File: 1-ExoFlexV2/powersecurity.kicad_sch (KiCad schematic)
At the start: 21 parts, among them J1 24V, J3 24V, K1 UD2-5NU, U1 PTSM36ADBZR, U3 STPS20M100SG-TR, U4 SN74LVC3G14DCUT_V2, U5 CD4044BPWR

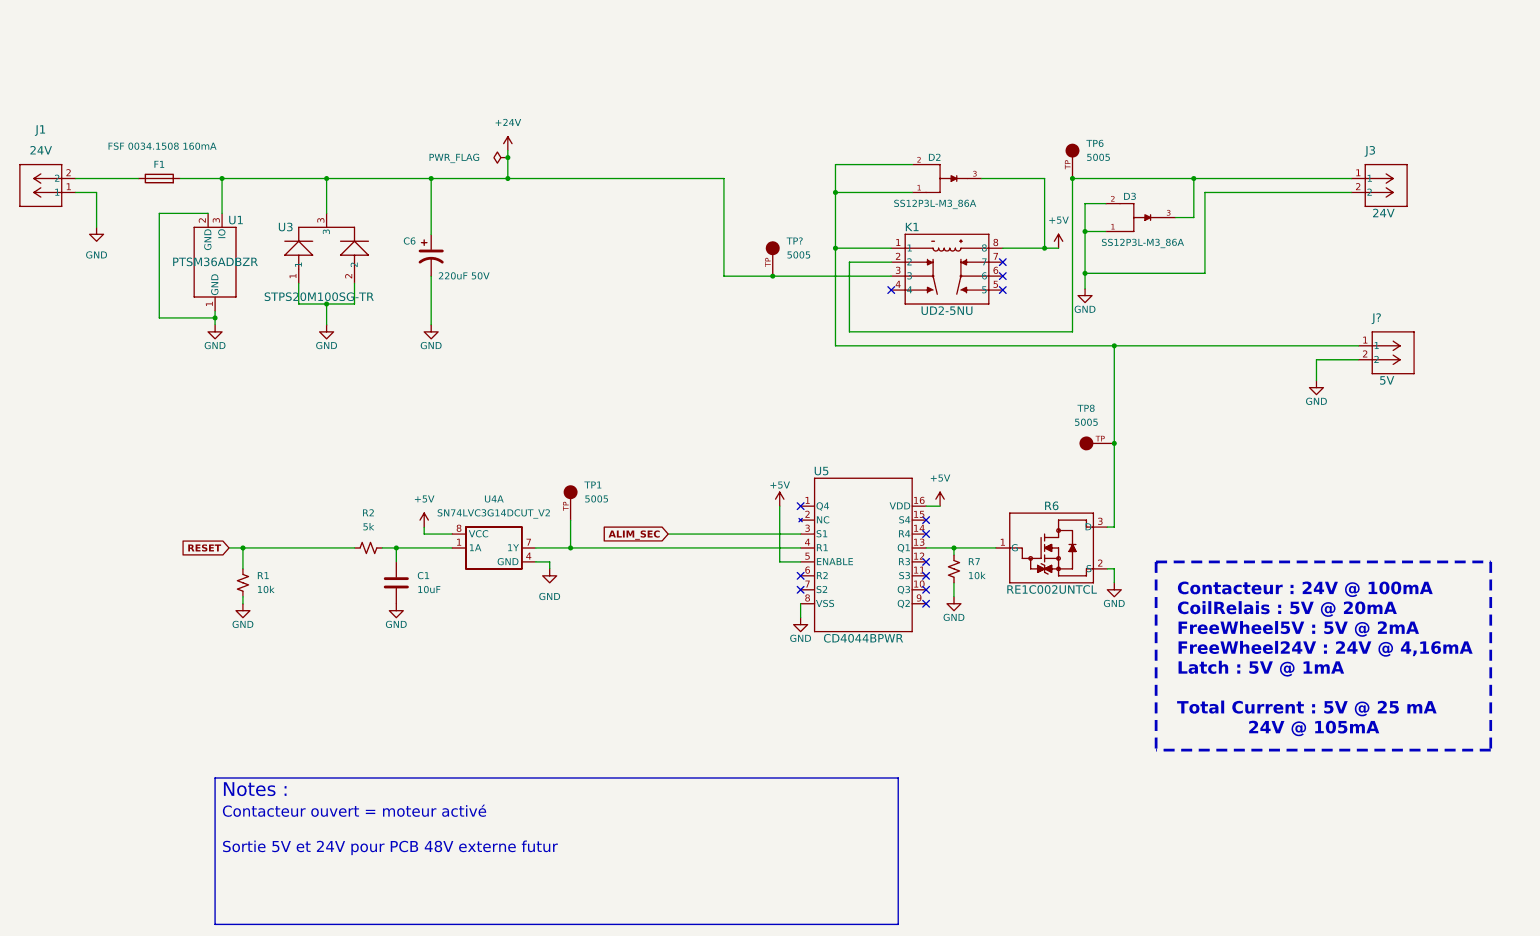
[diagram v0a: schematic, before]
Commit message: Chokes et RC
- Ajout des RF chokes
- Changement des résistance pour 0805
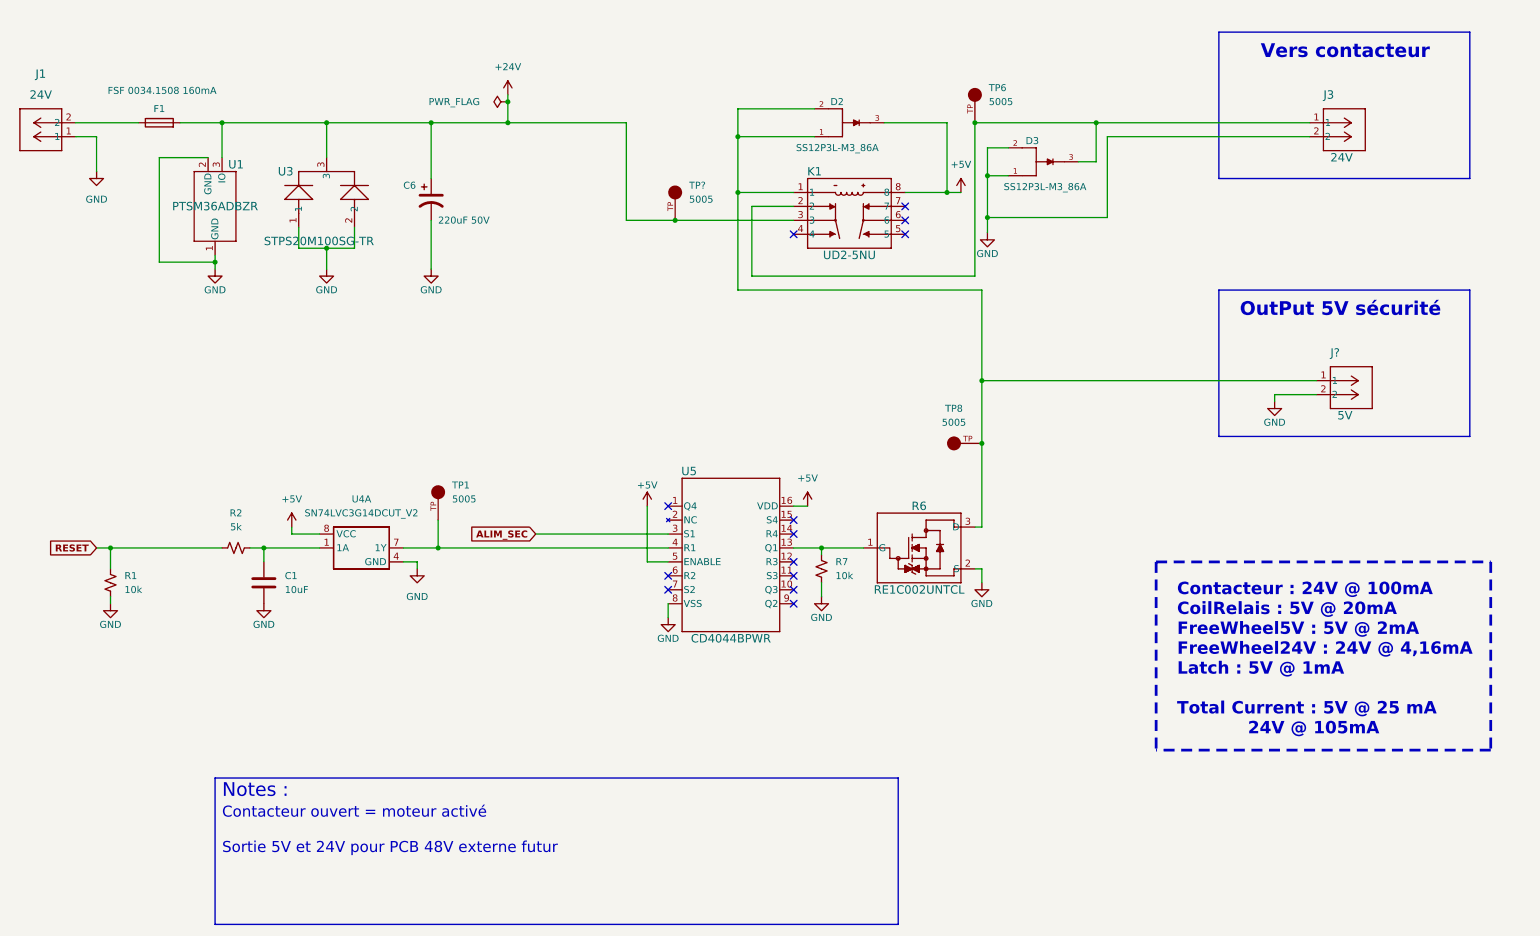
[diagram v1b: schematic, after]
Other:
- note added: "OutPut 5V sécurité"
- note added: "Vers contacteur"
- moved on the sheet: C1, C6, D2, D3, F1, J1, J3, J?, K1, R1, R2, R6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

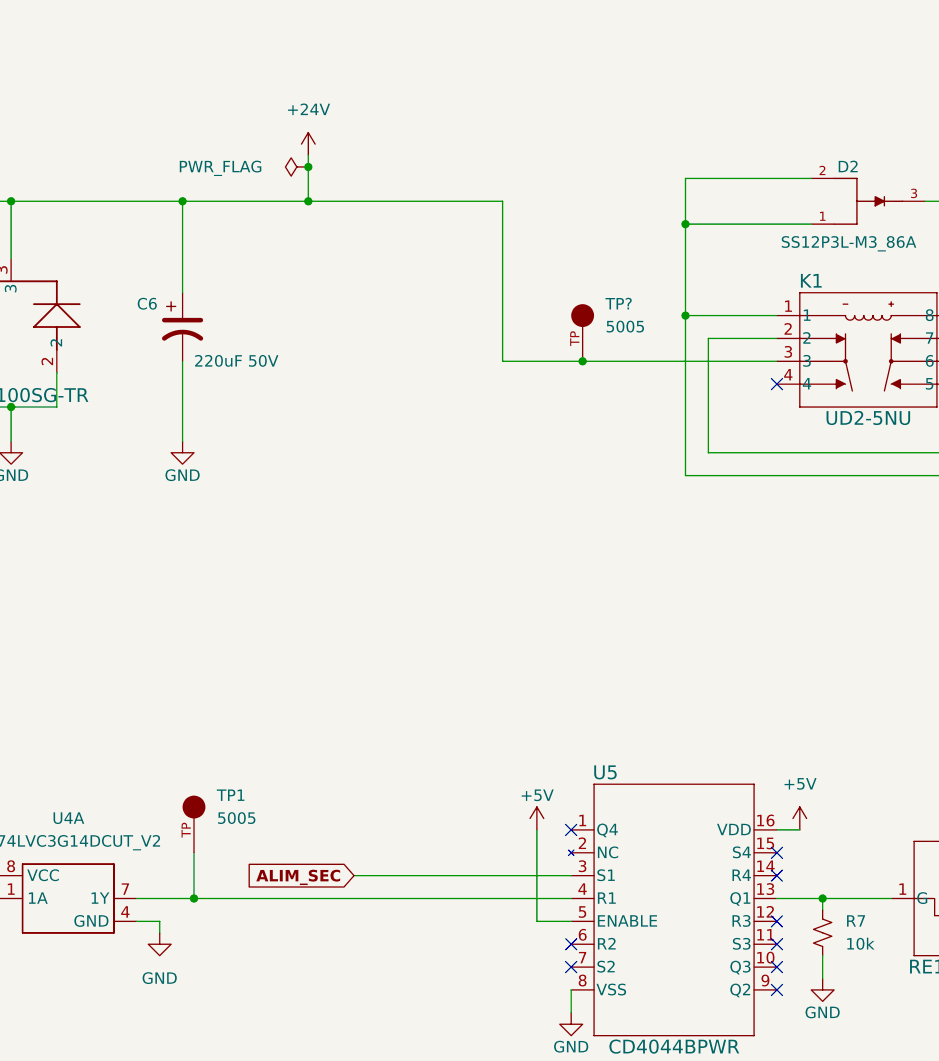
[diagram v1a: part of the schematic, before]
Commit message: Trimmer et jumper
-Changement de symbole de jumper
-Ajout des des trimmer aux endroits nécessaires
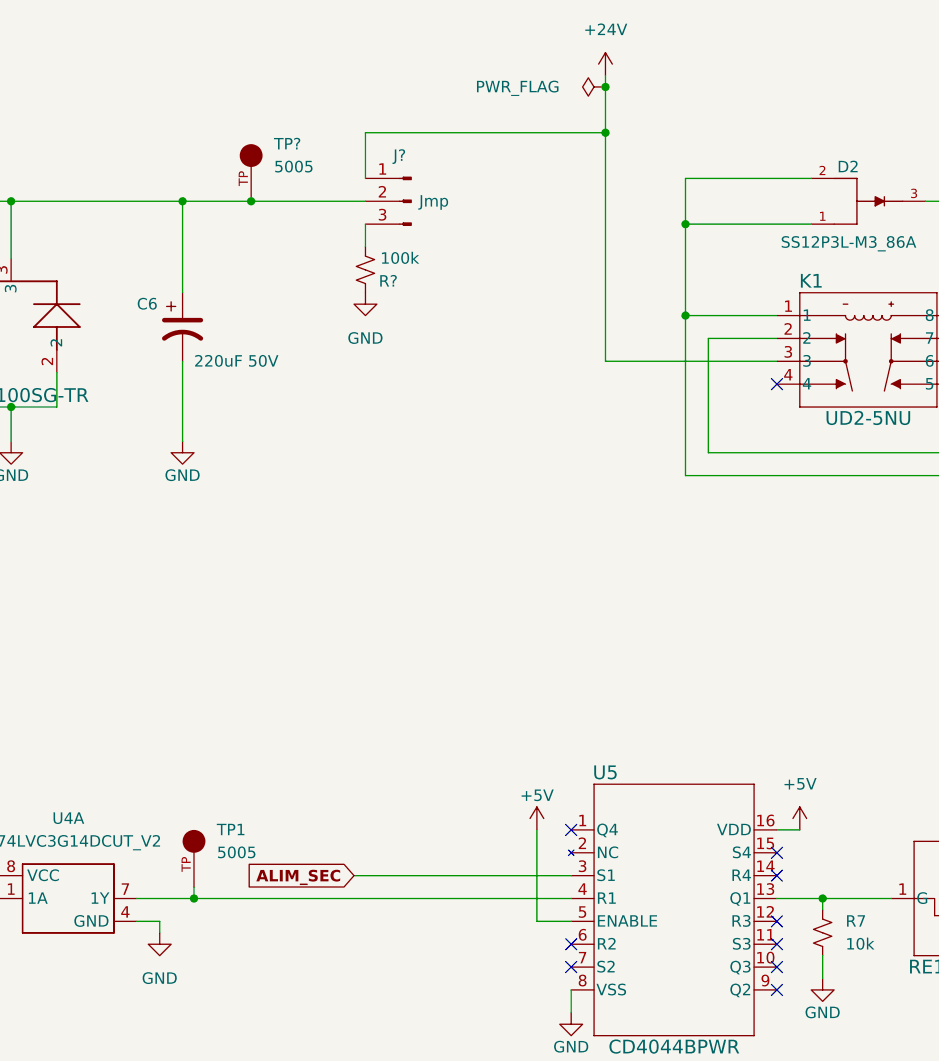
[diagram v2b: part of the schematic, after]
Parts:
- removed TP?: 5005, FootPrint:KEYSTONE_5005, symbol SymLib:5005
- added J?: Jmp, symbol Connector:Conn_01x03_Male
- added R?: 100k, Resistor_SMD:R_0805_2012Metric, symbol Device:R_Small_US
- added TP?: 5005, FootPrint:KEYSTONE_5005, symbol SymLib:5005
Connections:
- net +24V: now also J?.1 (Pin_1); no longer C6.1, F1.2, U1.3 (IO), U3.3
- net GND: now also R?.2
- new net: C6.1, F1.2, J?.2 (Pin_2), TP?.TP, U1.3 (IO), U3.3
- new net: J?.3 (Pin_3), R?.1
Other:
- moved on the sheet: TP1

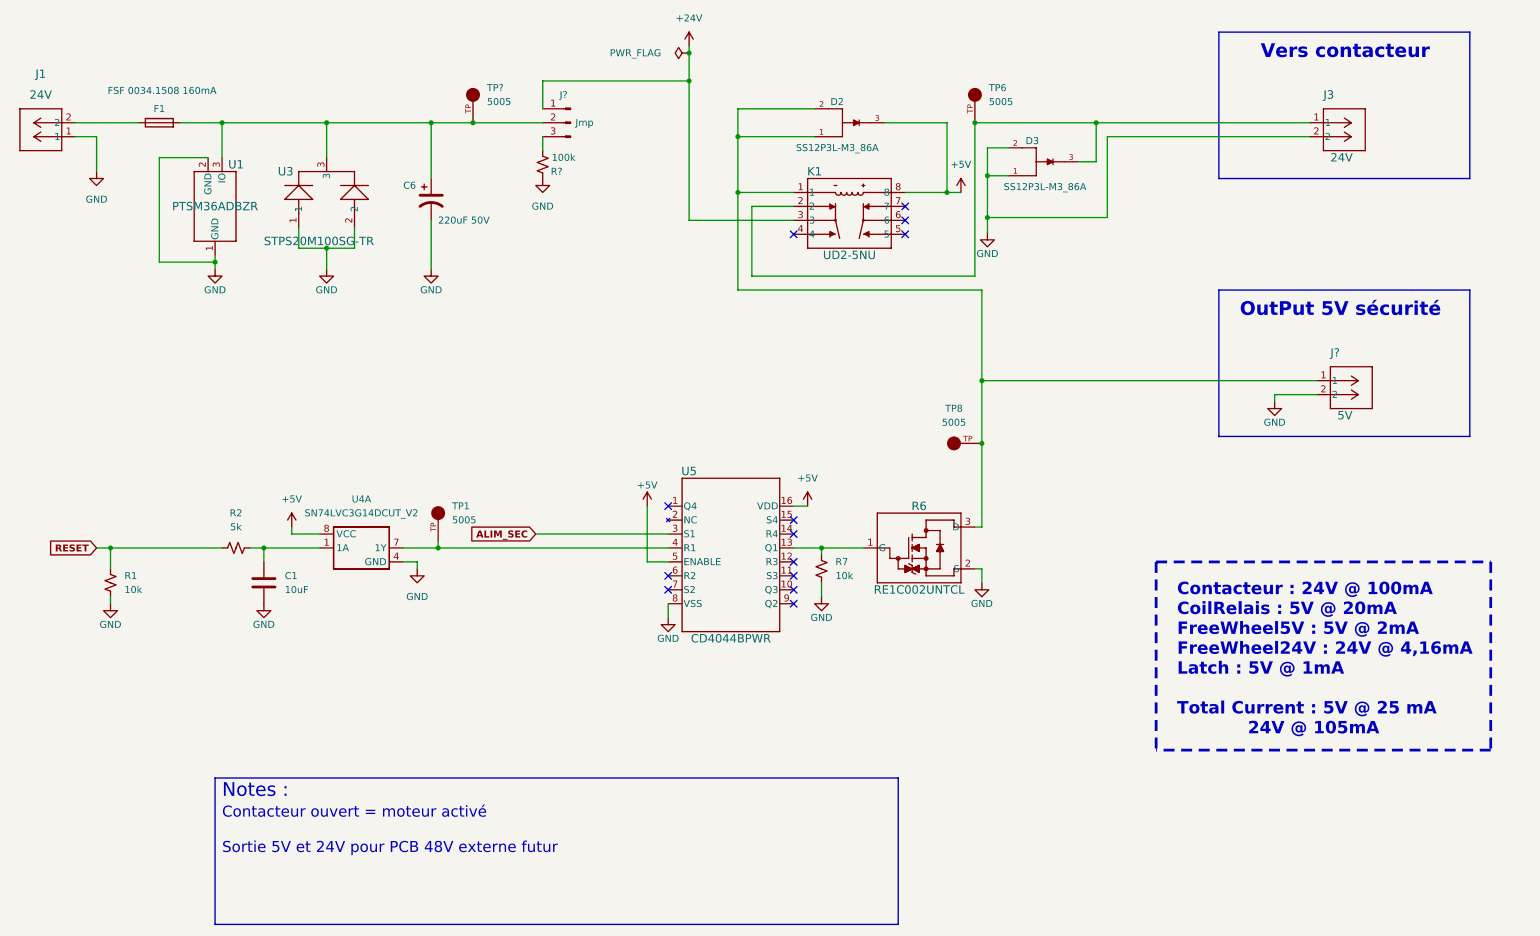
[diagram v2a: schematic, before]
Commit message: Test points et notes
- Ajout de tous les tests point nécessaires
-  Ajoute des sections de notes dans chaque page
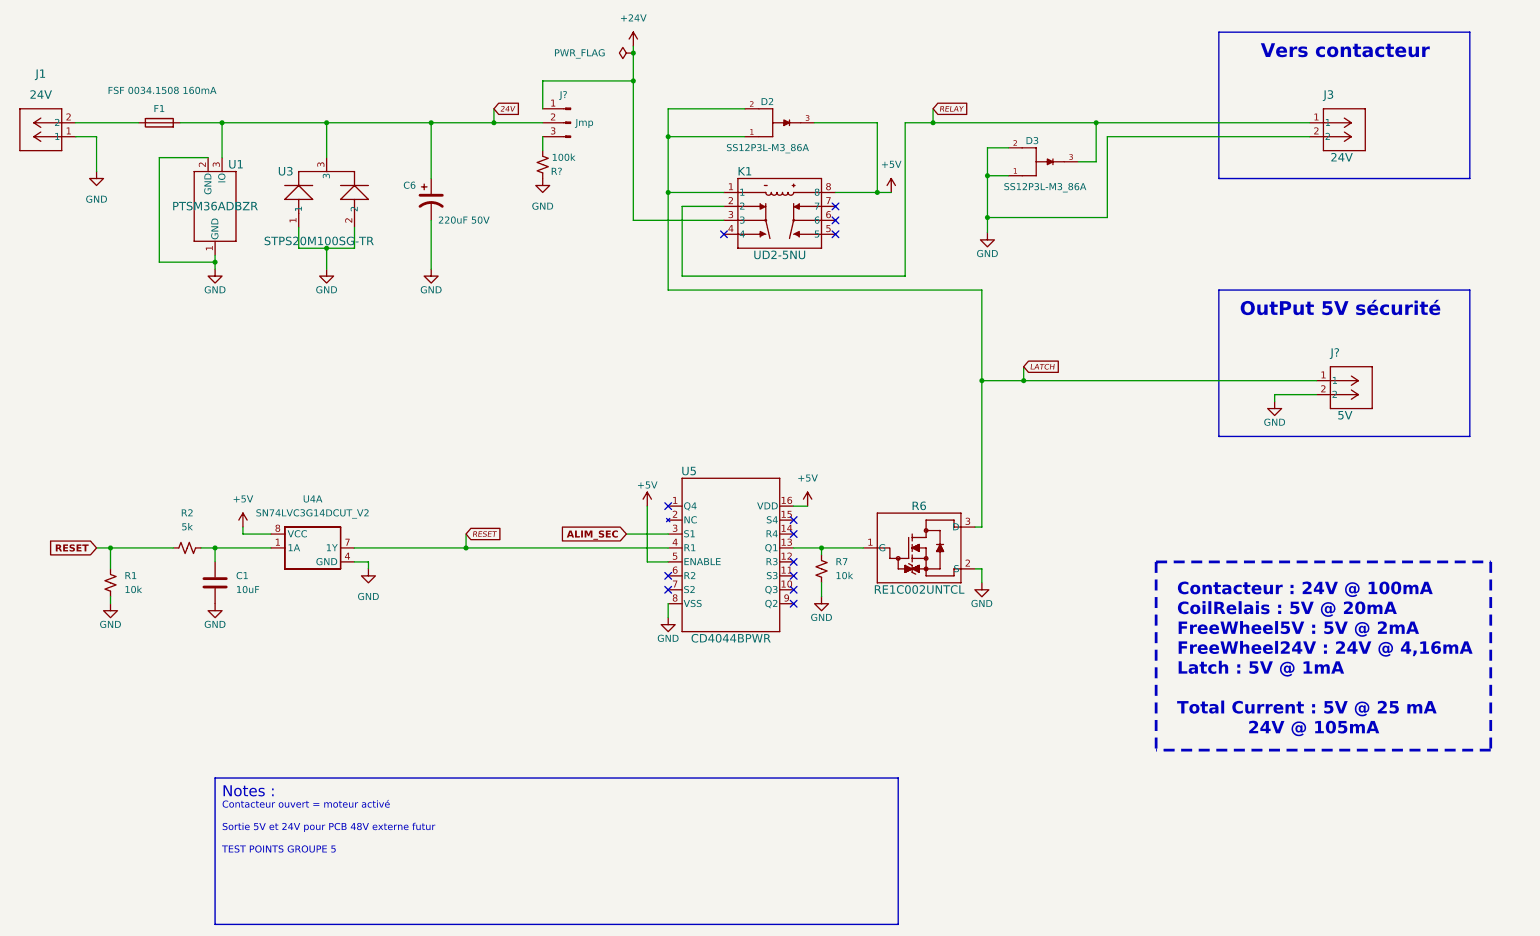
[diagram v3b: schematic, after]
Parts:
- removed TP1, TP6, TP8, TP?: 5005, FootPrint:KEYSTONE_5005, symbol SymLib:5005
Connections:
- net RESET: now also U4.7 (1Y), U5.4 (R1)
- net 24V: now reaches C6.1, F1.2, J?.2 (Pin_2), U1.3 (IO), U3.3
- net RELAY: now reaches D3.3, J3.1, K1.2
- net LATCH: now reaches D2.1, D2.2, J?.1, K1.1, R6.3 (D)
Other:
- note added: "Contacteur ouvert = moteur activé Sortie 5V et 24V pour PCB 48V externe futur TEST POINTS GROUPE 5"
- note removed: "Contacteur ouvert = moteur activé Sortie 5V et 24V pour PCB 48V externe futur"
- moved on the sheet: C1, D2, K1, R2, U4A

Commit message: Schématisation terminée
- Schéma terminé
- Passage vers le PCB
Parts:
- removed R7: 10k, Resistor_SMD:R_0603_1608Metric, symbol Device:R_Small_US
- added R4: 10k 5% 1/8W, Resistor_SMD:R_0805_2012Metric, symbol Device:R_Small_US
- C1: value 10uF -> 10uF 10V X7R; footprint Capacitor_SMD:C_0603_1608Metric -> Capacitor_SMD:C_0805_2012Metric; DESCRIPTION (none) -> 10 µF ±10% 10V Ceramic Capacitor X7R 0805 (2012 Metric); MANUFACTURER (none) -> Murata Electronics; PACKAGE (none) -> 0805 (2012 Metric); PART NUMBER (none) -> GRM21BR71A106KA73L; TYPE (none) -> SMD
- C2: renamed from C6; value 220uF 50V -> 220uF 20% 50V; DESCRIPTION (none) -> 220 µF 50 V Aluminum - Polymer Capacitors Radial, Can - SMD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; MANUFACTURER (none) -> Panasonic Electronic Components; PACKAGE (none) -> Radial, Can; PART NUMBER (none) -> EEH-ZS1H221P; TYPE (none) -> SMD
- D1: renamed from D2; value SS12P3L-M3_86A -> SHOTT 30V 12A; DESCRIPTION (none) -> Diode 30 V 12A Surface Mount TO-277A (SMPC); MANUFACTURER VISHAY -> Vishay General Semiconductor - Diodes Division; PACKAGE (none) -> TO-277, 3-PowerDFN; PART NUMBER (none) -> SS12P3L-M3/86A; TYPE (none) -> SMD
- D2: renamed from D3; value SS12P3L-M3_86A -> SHOTT 30V 12A; DESCRIPTION (none) -> Diode 30 V 12A Surface Mount TO-277A (SMPC); MANUFACTURER VISHAY -> Vishay General Semiconductor - Diodes Division; PACKAGE (none) -> TO-277, 3-PowerDFN; PART NUMBER (none) -> SS12P3L-M3/86A; TYPE (none) -> SMD
- F1: value FSF 0034.1508 160mA -> Fuse; DESCRIPTION (none) -> Fuse Block 20 A 250V 1 Circuit Cartridge Through Hole; MANUFACTURER (none) -> Würth Elektronik; NOTES (none) -> USE WITH 0034.1508; PACKAGE (none) -> 1 Circuit Cartridge; PART NUMBER (none) -> 696108003002; TYPE (none) -> Through Hole
- J1, J3: value 24V -> 14 AWG; DESCRIPTION (none) -> 2 Position Wire to Board Terminal Block Horizontal with Boa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; MANUFACTURER (none) -> Phoenix Contact; PACKAGE (none) -> 2 POS 0.200" (5.08mm); PART NUMBER (none) -> 1729128; TYPE (none) -> Through Hole
- J2: renamed from J?; value Jmp -> Jumper; footprint (none) -> Connector_PinSocket_2.54mm:PinSocket_1x03_P2.54mm_Vertical; DESCRIPTION (none) -> CONN HEADER VERT 3POS 2.54MM; MANUFACTURER (none) -> Würth Elektronik; PACKAGE (none) -> Square 0.100" (2.54mm); PART NUMBER (none) -> 61300311121; TYPE (none) -> Through Hole
- J4: renamed from J?; value 5V -> 14 AWG; DESCRIPTION (none) -> 2 Position Wire to Board Terminal Block Horizontal with Boa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; MANUFACTURER (none) -> Phoenix Contact; PACKAGE (none) -> 2 POS 0.200" (5.08mm); PART NUMBER (none) -> 1729128; TYPE (none) -> Through Hole
- K1: value UD2-5NU -> Relay; DESCRIPTION (none) -> General Purpose Relay DPDT (2 Form C) Surface Mount; MANUFACTURER (none) -> KEMET; PACKAGE (none) -> DPDT (2 Form C); PART NUMBER (none) -> UD2-5NU; TYPE (none) -> SMD
- Q1: renamed from R6; value RE1C002UNTCL -> MOSFET 20V 200mA; DESCRIPTION (none) -> N-Channel 20 V 200mA (Ta) 150mW (Ta) Surface Mount EMT3F (S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; MANUFACTURER (none) -> Rohm Semiconductor; PACKAGE (none) -> SC-89, SOT 490; PART NUMBER (none) -> RE1C002UNTCL; TYPE (none) -> SMD
- R1: value 10k -> 10k 5% 1/8W; footprint Resistor_SMD:R_0603_1608Metric -> Resistor_SMD:R_0805_2012Metric; DESCRIPTION (none) -> 10 kOhms ±5% 0.125W, 1/8W Chip Resistor 0805 (2012 Metric) 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; MANUFACTURER (none) -> Panasonic Electronic Components; PACKAGE (none) -> 0805 (2012 Metric); PART NUMBER (none) -> ERJ-6GEYJ103V; TYPE (none) -> SMD
- R2: value 5k -> 0Ω; footprint Resistor_SMD:R_0603_1608Metric -> Resistor_SMD:R_0805_2012Metric; DESCRIPTION (none) -> 0 Ohms Jumper Chip Resistor 0805 (2012 Metric) Automotive A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; MANUFACTURER (none) -> Panasonic Electronic Components; PACKAGE (none) -> 0805 (2012 Metric); PART NUMBER (none) -> ERJ-6GEY0R00V; TYPE (none) -> SMD
- R3: renamed from R?; value 100k -> 100k 5% 1/8W; DESCRIPTION (none) -> 100 kOhms ±5% 0.125W, 1/8W Chip Resistor 0805 (2012 Metric)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; MANUFACTURER (none) -> Panasonic Electronic Components; PACKAGE (none) -> 0805 (2012 Metric); PART NUMBER (none) -> ERJ-6GEYJ104V; TYPE (none) -> SMD
- U1: value PTSM36ADBZR -> TVS 24V; DESCRIPTION (none) -> 57V (Typ) Clamp 41A (8/20µs) Ipp Tvs Diode Surface Mount SO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; MANUFACTURER (none) -> Texas Instruments; PACKAGE (none) -> SOT-23-3; PART NUMBER (none) -> TSM36ADBZR; TYPE (none) -> SMD
- U2: renamed from U3; value STPS20M100SG-TR -> Shott 100V; DESCRIPTION (none) -> Diode 100 V 20A Surface Mount D2PAK; MANUFACTURER (none) -> STMicroelectronics; PACKAGE (none) -> TO-263-3, D2PAK (2 Leads + Tab), TO-263AB; PART NUMBER (none) -> STPS20M100SG-TR; TYPE (none) -> SMD
- U3: renamed from U4; value SN74LVC3G14DCUT_V2 -> Inverter; DESCRIPTION (none) -> Inverter IC 3 Channel Schmitt Trigger 8-VSSOP; MANUFACTURER (none) -> Texas Instruments; PACKAGE (none) -> 8-VFSOP (0.091", 2.30mm Width); PART NUMBER (none) -> SN74LVC3G14DCUT; TYPE (none) -> SMD
- U4: renamed from U5; value CD4044BPWR -> SR-Latch; DESCRIPTION (none) -> S-R Latch 4 Channel 1:1 IC Tri-State 16-TSSOP; MANUFACTURER (none) -> Texas Instruments; PACKAGE (none) -> 16-TSSOP (0.173", 4.40mm Width); PART NUMBER (none) -> CD4044BPWR; TYPE (none) -> SMD
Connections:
- net GND: now also R4.2
- net at Q1.1 (G), U4.13 (Q1): now also R4.1
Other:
- note added: "24V"
- note added: "Vers contacteur 24V"
- note removed: "Vers contacteur"
- moved on the sheet: U4
